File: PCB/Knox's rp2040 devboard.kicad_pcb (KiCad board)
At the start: 2 copper layers, 21 x 51 mm, 33 parts, among them J1 USB_C_Receptacle_USB2.0_14P, J2 Conn_01x20, J3 Conn_01x20, J4 Conn_01x03, SW1 SW_Push, U1 RP2040, U2 MCP1700x-330xxTT, U4 W25Q16JVZPIQ TR, Y1 12 MHz

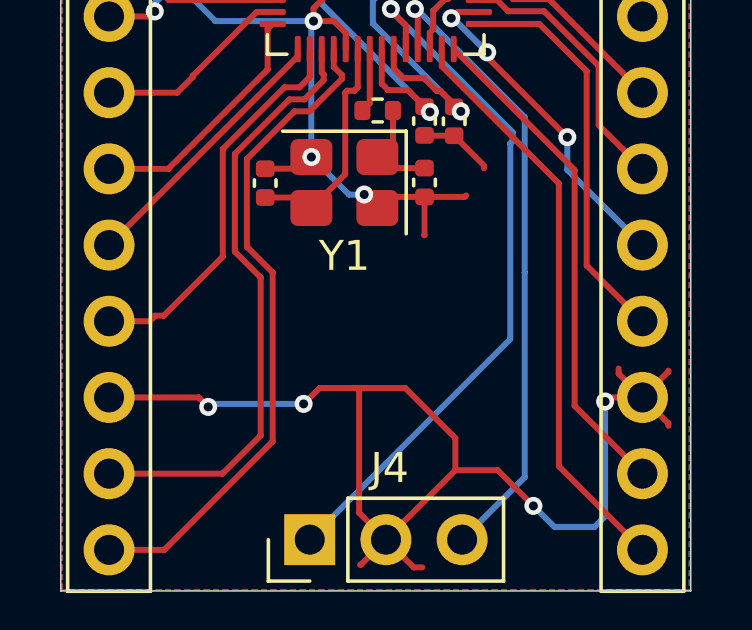
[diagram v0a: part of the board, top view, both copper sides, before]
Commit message: added image to pcb
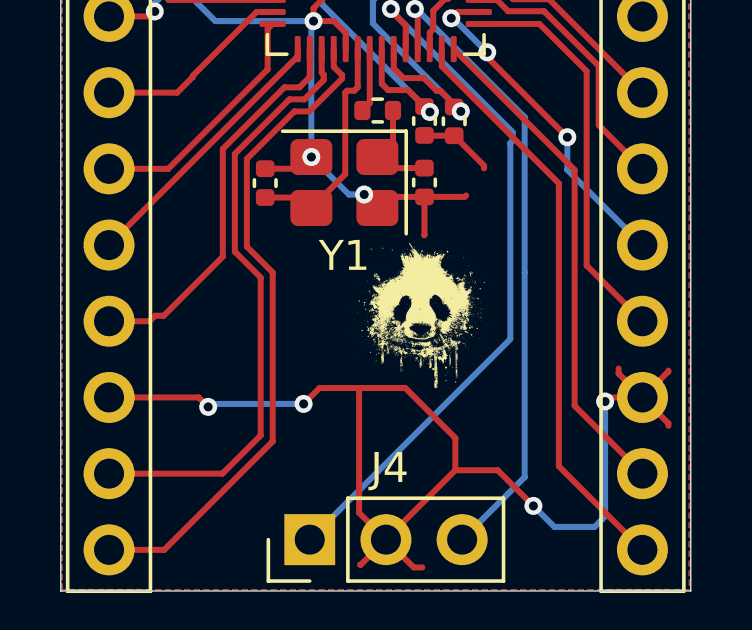
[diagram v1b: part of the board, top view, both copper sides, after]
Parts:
- added G***: LOGO, Pictures:panda1, F.Cu at (188.8, 98.5)
